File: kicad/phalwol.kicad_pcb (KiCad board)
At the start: 2 copper layers, 169.6 x 116.9 mm, 68 parts

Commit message: update pcb and schema
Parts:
- added REF**: D, yubuGadgetsFootpints:Diode_TH_SMD_REVERSIBLE, F.Cu at (134.7, 114.8)
- added REF**: D, yubuGadgetsFootpints:Diode_TH_SMD_REVERSIBLE, F.Cu at (106.2, 98.2)
- added REF**: D, yubuGadgetsFootpints:Diode_TH_SMD_REVERSIBLE, F.Cu at (134.8, 117.2)
- added REF**: D, yubuGadgetsFootpints:Diode_TH_SMD_REVERSIBLE, F.Cu at (158.5, 60.2)
- added REF**: D, yubuGadgetsFootpints:Diode_TH_SMD_REVERSIBLE, F.Cu at (144.2, 76.8)
- added REF**: D, yubuGadgetsFootpints:Diode_TH_SMD_REVERSIBLE, F.Cu at (101.5, 60.2)
- added REF**: D, yubuGadgetsFootpints:Diode_TH_SMD_REVERSIBLE, F.Cu at (182.2, 79.2)
- added REF**: D, yubuGadgetsFootpints:Diode_TH_SMD_REVERSIBLE, F.Cu at (144.2, 79.2)
- added REF**: D, yubuGadgetsFootpints:Diode_TH_SMD_REVERSIBLE, F.Cu at (125.2, 95.8)
- added REF**: D, yubuGadgetsFootpints:Diode_TH_SMD_REVERSIBLE, F.Cu at (139.5, 60.2)
- added REF**: D, yubuGadgetsFootpints:Diode_TH_SMD_REVERSIBLE, F.Cu at (106.2, 79.2)
- added REF**: D, yubuGadgetsFootpints:Diode_TH_SMD_REVERSIBLE, F.Cu at (101.5, 57.8)
- added REF**: D, yubuGadgetsFootpints:Diode_TH_SMD_REVERSIBLE, F.Cu at (163.2, 79.2)
- added REF**: D, yubuGadgetsFootpints:Diode_TH_SMD_REVERSIBLE, F.Cu at (172.8, 117.2)
- added REF**: D, yubuGadgetsFootpints:Diode_TH_SMD_REVERSIBLE, F.Cu at (144.2, 95.8)
- added REF**: D, yubuGadgetsFootpints:Diode_TH_SMD_REVERSIBLE, F.Cu at (106.2, 95.8)
- added REF**: D, yubuGadgetsFootpints:Diode_TH_SMD_REVERSIBLE, F.Cu at (120.5, 60.2)
- added REF**: D, yubuGadgetsFootpints:Diode_TH_SMD_REVERSIBLE, F.Cu at (177.5, 57.8)
- added REF**: D, yubuGadgetsFootpints:Diode_TH_SMD_REVERSIBLE, F.Cu at (125.2, 76.8)
- added REF**: D, yubuGadgetsFootpints:Diode_TH_SMD_REVERSIBLE, F.Cu at (158.5, 57.8)
- added REF**: D, yubuGadgetsFootpints:Diode_TH_SMD_REVERSIBLE, F.Cu at (163.2, 95.8)
- added REF**: D, yubuGadgetsFootpints:Diode_TH_SMD_REVERSIBLE, F.Cu at (153.8, 117.2)
- added REF**: D, yubuGadgetsFootpints:Diode_TH_SMD_REVERSIBLE, F.Cu at (191.7, 114.8)
- added REF**: D, yubuGadgetsFootpints:Diode_TH_SMD_REVERSIBLE, F.Cu at (177.5, 60.2)
- added REF**: D, yubuGadgetsFootpints:Diode_TH_SMD_REVERSIBLE, F.Cu at (172.7, 114.8)
- added REF**: D, yubuGadgetsFootpints:Diode_TH_SMD_REVERSIBLE, F.Cu at (139.5, 57.8)
- added REF**: D, yubuGadgetsFootpints:Diode_TH_SMD_REVERSIBLE, F.Cu at (153.7, 114.8)
- added REF**: D, yubuGadgetsFootpints:Diode_TH_SMD_REVERSIBLE, F.Cu at (182.2, 76.8)
- added REF**: D, yubuGadgetsFootpints:Diode_TH_SMD_REVERSIBLE, F.Cu at (106.2, 76.8)
- added REF**: D, yubuGadgetsFootpints:Diode_TH_SMD_REVERSIBLE, F.Cu at (115.7, 114.8)
- added REF**: D, yubuGadgetsFootpints:Diode_TH_SMD_REVERSIBLE, F.Cu at (120.5, 57.8)
- added REF**: D, yubuGadgetsFootpints:Diode_TH_SMD_REVERSIBLE, F.Cu at (144.2, 98.2)
- added REF**: D, yubuGadgetsFootpints:Diode_TH_SMD_REVERSIBLE, F.Cu at (163.2, 76.8)
- added REF**: D, yubuGadgetsFootpints:Diode_TH_SMD_REVERSIBLE, F.Cu at (163.2, 98.2)
- added REF**: D, yubuGadgetsFootpints:Diode_TH_SMD_REVERSIBLE, F.Cu at (115.8, 117.2)
- added REF**: D, yubuGadgetsFootpints:Diode_TH_SMD_REVERSIBLE, F.Cu at (182.2, 98.2)
- added REF**: D, yubuGadgetsFootpints:Diode_TH_SMD_REVERSIBLE, F.Cu at (125.2, 79.2)
- added REF**: D, yubuGadgetsFootpints:Diode_TH_SMD_REVERSIBLE, F.Cu at (182.2, 95.8)
- added REF**: D, yubuGadgetsFootpints:Diode_TH_SMD_REVERSIBLE, F.Cu at (125.2, 98.2)

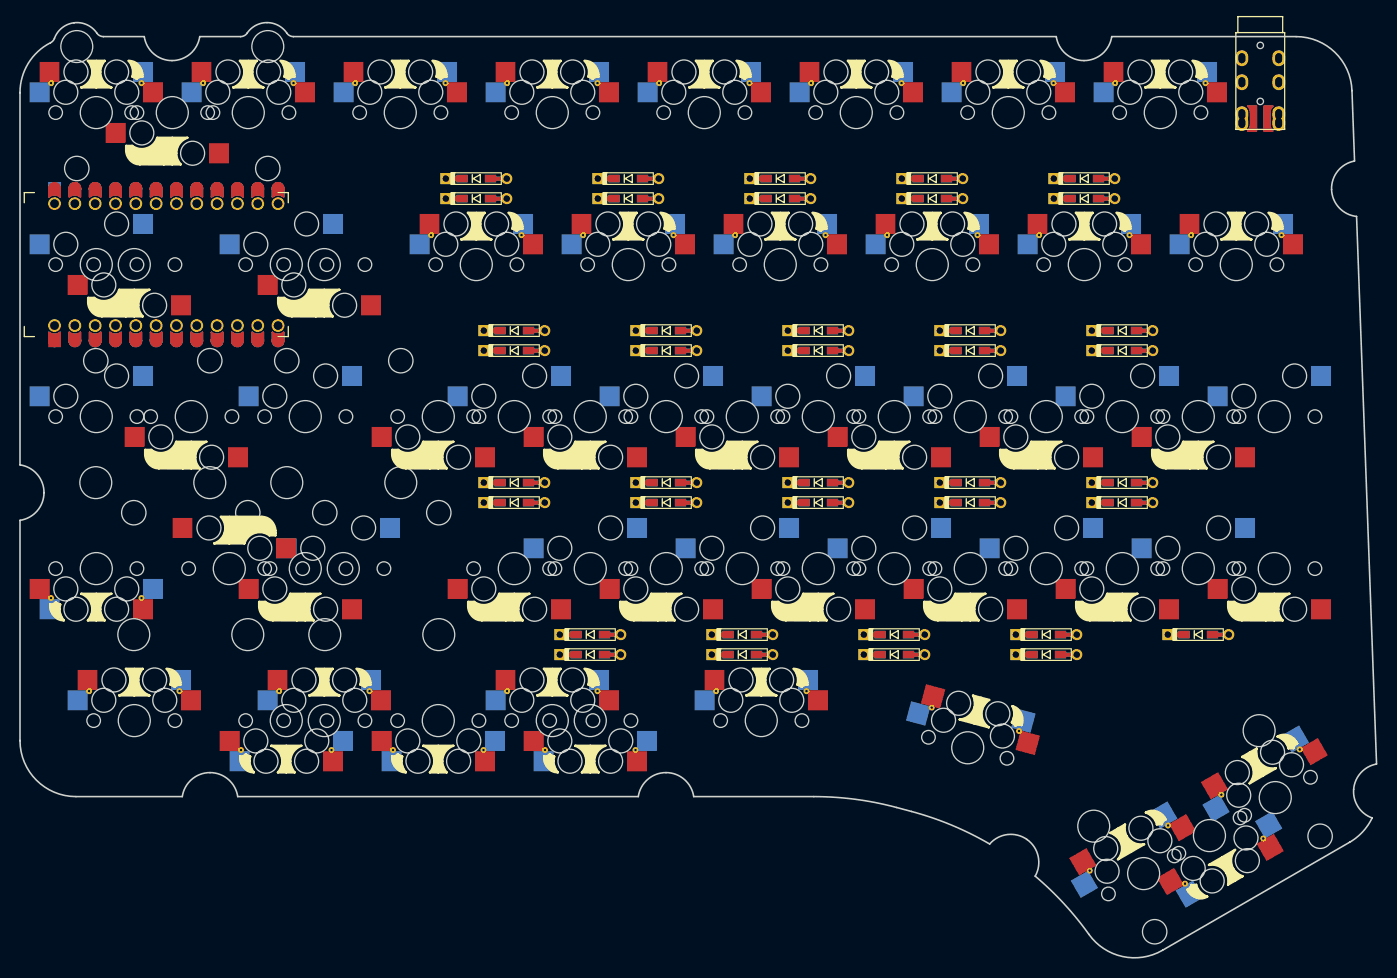
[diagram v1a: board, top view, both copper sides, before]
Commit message: connect schema and pcb
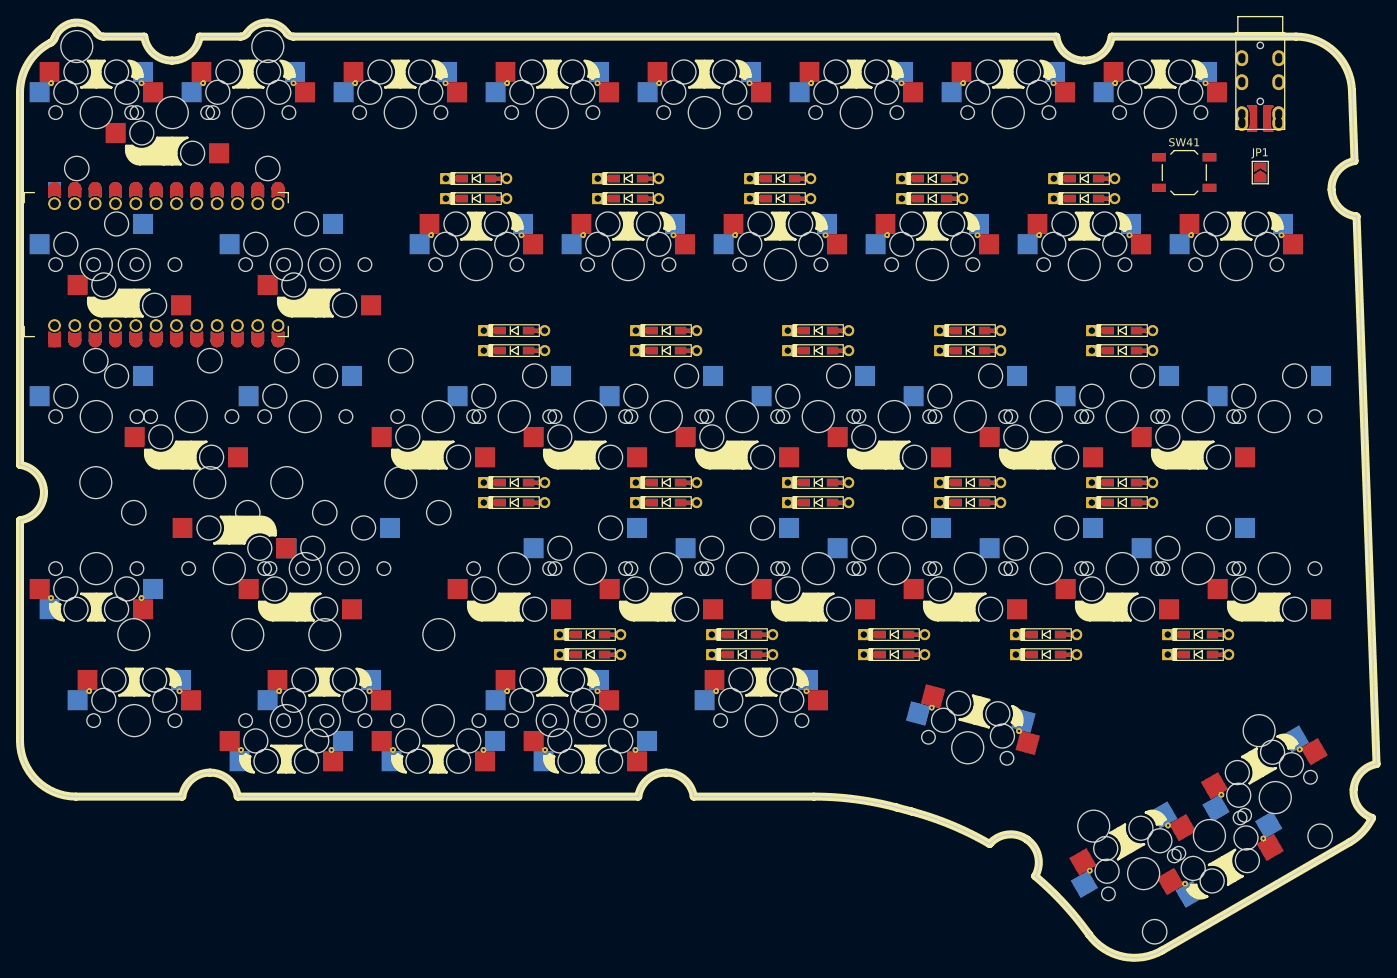
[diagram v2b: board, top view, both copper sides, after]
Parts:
- added D40: D, yubuGadgetsFootpints:Diode_TH_SMD_REVERSIBLE, F.Cu at (191.8, 117.2)
- added JP1: SolderJumper_2_Open, Jumper:SolderJumper-2_P1.3mm_Open_TrianglePad1.0x1.5mm, F.Cu at (199.5, 57.0)
- added JP2: SolderJumper_2_Open, Jumper:SolderJumper-2_P1.3mm_Open_TrianglePad1.0x1.5mm, B.Cu at (199.5, 57.0)
- added SW41: SW_Push, Button_Switch_SMD:SW_SPST_TL3342, F.Cu at (190.0, 57.0)
- added SW41: SW_Push, Button_Switch_SMD:SW_SPST_TL3342, B.Cu at (190.0, 57.0)
- J1: renamed from REF**; value TRRS-PJ-320A-ReversiblePad -> AudioJack4
- SW1 (x2), SW10 (x2), SW11, SW12, SW13, SW14, SW15, SW16, SW17 (x2), SW18, SW19 (x2), SW2, SW20 (x2), SW21 (x2), SW22 (x2), SW23 (x2), SW24 (x2), SW25, SW26 (x2), SW27 (x2), SW28 (x2), SW29 (x2), SW3, SW30 (x2), SW31 (x2), SW32, SW33, SW34 (x2), SW35 (x2), SW36, SW37, SW38, SW39 (x2), SW4, SW40, SW5, SW6, SW7, SW8, SW9 (x2): renamed from S*; value Val** -> SW_Push
- SW26: renamed from REF**; value Val** -> SW_Push
- renumbered REF** to D1, REF** to D10, REF** to D11, REF** to D12, REF** to D13, REF** to D14, REF** to D15, REF** to D16, REF** to D17, REF** to D18, REF** to D19, REF** to D2, REF** to D20, REF** to D21, REF** to D22, REF** to D23, REF** to D24, REF** to D25, REF** to D26, REF** to D27, REF** to D28, REF** to D29, REF** to D3, REF** to D30, REF** to D31, REF** to D32, REF** to D33, REF** to D34, REF** to D35, REF** to D36, REF** to D37, REF** to D38, REF** to D39, REF** to D4, REF** to D5, REF** to D6, REF** to D7, REF** to D8, REF** to D9, REF** to U1
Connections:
- D1 pad 1: (no net) -> ROW1
- D1 pad 2: (no net) -> Net-(D1-A)
- D10 pad 1: (no net) -> ROW2
- D10 pad 2: (no net) -> Net-(D10-A)
- D11 pad 1: (no net) -> ROW2
- D11 pad 2: (no net) -> Net-(D11-A)
- D12 pad 1: (no net) -> ROW2
- D12 pad 2: (no net) -> Net-(D12-A)
- D13 pad 1: (no net) -> ROW2
- D13 pad 2: (no net) -> Net-(D13-A)
- D14 pad 1: (no net) -> ROW2
- D14 pad 2: (no net) -> Net-(D14-A)
- D15 pad 1: (no net) -> ROW2
- D15 pad 2: (no net) -> Net-(D15-A)
- D16 pad 1: (no net) -> ROW2
- D16 pad 2: (no net) -> Net-(D16-A)
- D17 pad 1: (no net) -> ROW3
- D17 pad 2: (no net) -> Net-(D17-A)
- D18 pad 1: (no net) -> ROW3
- D18 pad 2: (no net) -> Net-(D18-A)
- D19 pad 1: (no net) -> ROW3
- D19 pad 2: (no net) -> Net-(D19-A)
- D2 pad 1: (no net) -> ROW1
- D2 pad 2: (no net) -> Net-(D2-A)
- D20 pad 1: (no net) -> ROW3
- D20 pad 2: (no net) -> Net-(D20-A)
- D21 pad 1: (no net) -> ROW3
- D21 pad 2: (no net) -> Net-(D21-A)
- D22 pad 1: (no net) -> ROW3
- D22 pad 2: (no net) -> Net-(D22-A)
- D23 pad 1: (no net) -> ROW3
- D23 pad 2: (no net) -> Net-(D23-A)
- D24 pad 1: (no net) -> ROW3
- D24 pad 2: (no net) -> Net-(D24-A)
- D25 pad 1: (no net) -> ROW4
- D25 pad 2: (no net) -> Net-(D25-A)
- D26 pad 1: (no net) -> ROW4
- D26 pad 2: (no net) -> Net-(D26-A)
- D27 pad 1: (no net) -> ROW4
- D27 pad 2: (no net) -> Net-(D27-A)
- D28 pad 1: (no net) -> ROW4
- D28 pad 2: (no net) -> Net-(D28-A)
- D29 pad 1: (no net) -> ROW4
- D29 pad 2: (no net) -> Net-(D29-A)
- D3 pad 1: (no net) -> ROW1
- D3 pad 2: (no net) -> Net-(D3-A)
- D30 pad 1: (no net) -> ROW4
- D30 pad 2: (no net) -> Net-(D30-A)
- D31 pad 1: (no net) -> ROW4
- D31 pad 2: (no net) -> Net-(D31-A)
- D32 pad 1: (no net) -> ROW4
- D32 pad 2: (no net) -> Net-(D32-A)
- D33 pad 1: (no net) -> ROW5
- D33 pad 2: (no net) -> Net-(D33-A)
- D34 pad 1: (no net) -> ROW5
- D34 pad 2: (no net) -> Net-(D34-A)
- D35 pad 1: (no net) -> ROW5
- D35 pad 2: (no net) -> Net-(D35-A)
- D36 pad 1: (no net) -> ROW5
- D36 pad 2: (no net) -> Net-(D36-A)
- D37 pad 1: (no net) -> ROW5
- D37 pad 2: (no net) -> Net-(D37-A)
- D38 pad 1: (no net) -> ROW5
- D38 pad 2: (no net) -> Net-(D38-A)
- D39 pad 1: (no net) -> ROW5
- D39 pad 2: (no net) -> Net-(D39-A)
- D4 pad 1: (no net) -> ROW1
- D4 pad 2: (no net) -> Net-(D4-A)
- D5 pad 1: (no net) -> ROW1
- D5 pad 2: (no net) -> Net-(D5-A)
- D6 pad 1: (no net) -> ROW1
- D6 pad 2: (no net) -> Net-(D6-A)
- D7 pad 1: (no net) -> ROW1
- D7 pad 2: (no net) -> Net-(D7-A)
- D8 pad 1: (no net) -> ROW1
- D8 pad 2: (no net) -> Net-(D8-A)
- D9 pad 1: (no net) -> ROW2
- D9 pad 2: (no net) -> Net-(D9-A)
- J1 pad R1: (no net) -> VCC
- J1 pad R2: (no net) -> GND
- J1 pad S: (no net) -> GND
- J1 pad T: (no net) -> SERIAL
- SW1 pad 1: (no net) -> COL1 (x2)
- SW1 pad 2: (no net) -> Net-(D1-A) (x2)
- SW10 pad 1: (no net) -> COL2 (x2)
- SW10 pad 2: (no net) -> Net-(D10-A) (x2)
- SW11 pad 1: (no net) -> COL3
- SW11 pad 2: (no net) -> Net-(D11-A)
- SW12 pad 1: (no net) -> COL4
- SW12 pad 2: (no net) -> Net-(D12-A)
- SW13 pad 1: (no net) -> COL5
- SW13 pad 2: (no net) -> Net-(D13-A)
- SW14 pad 1: (no net) -> COL6
- SW14 pad 2: (no net) -> Net-(D14-A)
- SW15 pad 1: (no net) -> COL7
- SW15 pad 2: (no net) -> Net-(D15-A)
- SW16 pad 1: (no net) -> COL8
- SW16 pad 2: (no net) -> Net-(D16-A)
- SW17 pad 1: (no net) -> COL1 (x2)
- SW17 pad 2: (no net) -> Net-(D17-A) (x2)
- SW18 pad 1: (no net) -> COL2
- SW18 pad 2: (no net) -> Net-(D18-A)
- SW19 pad 1: (no net) -> COL3 (x2)
- SW19 pad 2: (no net) -> Net-(D19-A) (x2)
- SW2 pad 1: (no net) -> COL2
- SW2 pad 2: (no net) -> Net-(D2-A)
- SW20 pad 1: (no net) -> COL4 (x2)
- SW20 pad 2: (no net) -> Net-(D20-A) (x2)
- SW21 pad 1: (no net) -> COL5 (x2)
- SW21 pad 2: (no net) -> Net-(D21-A) (x2)
- SW22 pad 1: (no net) -> COL6 (x2)
- SW22 pad 2: (no net) -> Net-(D22-A) (x2)
- SW23 pad 1: (no net) -> COL7 (x2)
- SW23 pad 2: (no net) -> Net-(D23-A) (x2)
- SW24 pad 1: (no net) -> COL8 (x2)
- SW24 pad 2: (no net) -> Net-(D24-A) (x2)
- SW25 pad 1: (no net) -> COL1
- SW25 pad 2: (no net) -> Net-(D25-A)
- SW26 pad 1: (no net) -> COL2 (x3)
- SW26 pad 2: (no net) -> Net-(D26-A) (x3)
- SW27 pad 1: (no net) -> COL3 (x2)
- SW27 pad 2: (no net) -> Net-(D27-A) (x2)
- SW28 pad 1: (no net) -> COL4 (x2)
- SW28 pad 2: (no net) -> Net-(D28-A) (x2)
- SW29 pad 1: (no net) -> COL5 (x2)
- SW29 pad 2: (no net) -> Net-(D29-A) (x2)
- SW3 pad 1: (no net) -> COL3
- SW3 pad 2: (no net) -> Net-(D3-A)
- SW30 pad 1: (no net) -> COL6 (x2)
- SW30 pad 2: (no net) -> Net-(D30-A) (x2)
- SW31 pad 1: (no net) -> COL7 (x2)
- SW31 pad 2: (no net) -> Net-(D31-A) (x2)
- SW32 pad 1: (no net) -> COL8
- SW32 pad 2: (no net) -> Net-(D32-A)
- SW33 pad 1: (no net) -> COL1
- SW33 pad 2: (no net) -> Net-(D33-A)
- SW34 pad 1: (no net) -> COL2 (x2)
- SW34 pad 2: (no net) -> Net-(D34-A) (x2)
- SW35 pad 1: (no net) -> COL3 (x2)
- SW35 pad 2: (no net) -> Net-(D35-A) (x2)
- SW36 pad 1: (no net) -> COL4
- SW36 pad 2: (no net) -> Net-(D36-A)
- SW37 pad 1: (no net) -> COL5
- SW37 pad 2: (no net) -> Net-(D37-A)
- SW38 pad 1: (no net) -> COL6
- SW38 pad 2: (no net) -> Net-(D38-A)
- SW39 pad 1: (no net) -> COL7 (x2)
- SW39 pad 2: (no net) -> Net-(D39-A) (x2)
- SW4 pad 1: (no net) -> COL4
- SW4 pad 2: (no net) -> Net-(D4-A)
- SW40 pad 1: (no net) -> COL8
- SW40 pad 2: (no net) -> Net-(D40-A)
- SW5 pad 1: (no net) -> COL5
- SW5 pad 2: (no net) -> Net-(D5-A)
- SW6 pad 1: (no net) -> COL6
- SW6 pad 2: (no net) -> Net-(D6-A)
- SW7 pad 1: (no net) -> COL7
- SW7 pad 2: (no net) -> Net-(D7-A)
- SW8 pad 1: (no net) -> COL8
- SW8 pad 2: (no net) -> Net-(D8-A)
- SW9 pad 1: (no net) -> COL1 (x2)
- SW9 pad 2: (no net) -> Net-(D9-A) (x2)
- U1 pad 1: (no net) -> unconnected-(U1-TX0/D3-Pad1)
- U1 pad 10: (no net) -> ROW3
- U1 pad 11: (no net) -> ROW2
- U1 pad 12: (no net) -> ROW1
- U1 pad 13: (no net) -> COL1
- U1 pad 14: (no net) -> COL2
- U1 pad 15: (no net) -> COL3
- U1 pad 16: (no net) -> COL4
- U1 pad 17: (no net) -> COL5
- U1 pad 18: (no net) -> COL6
- U1 pad 19: (no net) -> COL7
- U1 pad 2: (no net) -> SERIAL
- U1 pad 20: (no net) -> COL8
- U1 pad 21: (no net) -> VCC
- U1 pad 22: (no net) -> RST
- U1 pad 23: (no net) -> GND
- U1 pad 24: (no net) -> unconnected-(U1-RAW-Pad24)
- U1 pad 3: (no net) -> GND
- U1 pad 4: (no net) -> GND
- U1 pad 5: (no net) -> unconnected-(U1-2/D1/SDA-Pad5)
- U1 pad 6: (no net) -> unconnected-(U1-3/D0/SCL-Pad6)
- U1 pad 7: (no net) -> HAND
- U1 pad 8: (no net) -> ROW5
- U1 pad 9: (no net) -> ROW4

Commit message: update pcb
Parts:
- SW1, SW10 (x2), SW17 (x2), SW18, SW19 (x2), SW20 (x2), SW21 (x2), SW22 (x2), SW23 (x2), SW24 (x2), SW26 (x3), SW27 (x2), SW28 (x2), SW29 (x2), SW30 (x2), SW31 (x2), SW32, SW9 (x2): footprint yubuGadgetsFootpints:MX_HotswapOneside_Guided -> yubuGadgetsFootpints:MX_HotswapOneside_Via_Guided
- turned D1 to 180 degrees
- turned D10 to 180 degrees
- turned D11 to 180 degrees
- turned D12 to 180 degrees
- turned D13 to 180 degrees
- turned D14 to 180 degrees
- turned D15 to 180 degrees
- turned D16 to 180 degrees
- turned D17 to 180 degrees
- turned D18 to 180 degrees
- turned D19 to 180 degrees
- turned D2 to 180 degrees
- turned D20 to 180 degrees
- turned D21 to 180 degrees
- turned D22 to 180 degrees
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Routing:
- net COL1: track 0.00 -> 94.8 mm, vias 0 -> 1
- net ROW2: track 0.00 -> 58.1 mm, vias 0 -> 1
- net COL3: track 0.00 -> 57.1 mm, vias 0 -> 1
- net COL7: track 0.00 -> 55.7 mm, vias 0 -> 2
- net ROW3: track 0.00 -> 55.7 mm, vias 0 -> 1
- net ROW1: track 0.00 -> 54.7 mm, vias 0 -> 1
- net COL4: track 0.00 -> 54.0 mm, vias 0 -> 1
- net COL5: track 0.00 -> 51.8 mm, vias 0 -> 1
- net ROW4: track 0.00 -> 51.2 mm, vias 0 -> 1
- net COL6: track 0.00 -> 51.2 mm, vias 0 -> 1
- net ROW5: track 0.00 -> 50.6 mm, vias 0 -> 1
- net COL2: track 0.00 -> 39.3 mm, vias 0 -> 1
- net RST: track 0.00 -> 32.2 mm, vias 0 -> 1
- net VCC: track 0.00 -> 31.9 mm, vias 0 -> 1
- net unconnected-(U1-3/D0/SCL-Pad6): track 0.00 -> 23.9 mm, vias 0 -> 1
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
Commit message: Update phalwol.kicad_pcb
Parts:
- added SW26: SW_Push, yubuGadgetsFootpints:MX_HotswapOneside_Via_Guided, B.Cu at (75.4, 106.5)
- added SW27: SW_Push, yubuGadgetsFootpints:MX_HotswapOneside_Via_Guided, B.Cu at (96.8, 106.5)
- moved D8 100.3 mm to (196.5, 57.8)
- moved D7 97.4 mm to (196.5, 60.2)
- moved D6 82.0 mm to (177.5, 57.8)
- moved D5 79.6 mm to (177.5, 60.2)
- moved D16 77.9 mm to (201.2, 76.8)
- moved D15 75.4 mm to (201.2, 79.2)
- moved D25 73.3 mm to (115.8, 117.2)
- moved SW41 71.3 mm to (179.2, 127.5) (x2)
- moved D26 69.3 mm to (115.8, 114.8)
- moved D33 61.7 mm to (153.8, 114.8)
- moved D34 61.7 mm to (153.8, 117.2)
- moved D14 60.9 mm to (182.2, 76.8)
- moved D13 59.3 mm to (182.2, 79.2)
- moved D4 56.5 mm to (158.5, 57.8)
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- renumbered SW27 to SW28, SW28 to SW29, SW29 to SW30, SW30 to SW31, SW31 to SW32
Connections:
- SW28 pad 1: COL3 -> COL4
- SW28 pad 2: Net-(D27-A) -> Net-(D28-A)
- SW29 pad 1: COL4 -> COL5
- SW29 pad 2: Net-(D28-A) -> Net-(D29-A)
- SW30 pad 1: COL5 -> COL6
- SW30 pad 2: Net-(D29-A) -> Net-(D30-A)
- SW31 pad 1: COL6 -> COL7
- SW31 pad 2: Net-(D30-A) -> Net-(D31-A)
- SW32 pad 1: COL7 -> COL8
- SW32 pad 2: Net-(D31-A) -> Net-(D32-A)
- SW34 pad 1: COL2 -> Net-(D34-A)
- SW34 pad 2: Net-(D34-A) -> COL2
- SW35 pad 1: COL3 -> Net-(D35-A)
- SW35 pad 2: Net-(D35-A) -> COL3
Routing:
- net Net-(D9-A): track 9.21 -> 114.0 mm
- net Net-(D33-A): track 0.00 -> 89.2 mm, vias 1 -> 0
- net Net-(D1-A): track 13.1 -> 96.7 mm, vias 1 -> 0
- net Net-(D10-A): track 9.21 -> 83.3 mm
- net Net-(D35-A): track 0.00 -> 73.5 mm, vias 1 -> 0
- net Net-(D34-A): track 0.00 -> 73.2 mm, vias 1 -> 0
- net Net-(D36-A): track 0.00 -> 69.1 mm, vias 1 -> 0
- net Net-(D37-A): track 0.00 -> 64.7 mm, vias 1 -> 0
- net Net-(D3-A): track 0.00 -> 61.1 mm, vias 1 -> 0
- net Net-(D2-A): track 0.00 -> 60.1 mm, vias 1 -> 0
- net Net-(D11-A): track 0.00 -> 56.4 mm, vias 1 -> 0
- net Net-(D25-A): track 0.00 -> 54.4 mm, vias 1 -> 0
- net Net-(D17-A): track 16.3 -> 64.4 mm, vias 1 -> 0
- net Net-(D29-A): track 15.4 -> 60.8 mm, vias 1 -> 0
- net Net-(D5-A): track 0.00 -> 42.1 mm, vias 1 -> 0
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
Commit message: Update phalwol.kicad_pcb
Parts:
- moved JP1 0.39 mm to (205.8, 47.5)
- moved JP2 0.39 mm to (205.8, 47.5)
- moved D31 0.12 mm to (201.2, 95.8)
- moved D32 0.12 mm to (201.3, 98.2)
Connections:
- U1 pad 11: ROW2 -> ROW4
- U1 pad 12: ROW1 -> ROW5
- U1 pad 13: COL1 -> COL8
- U1 pad 14: COL2 -> COL7
- U1 pad 15: COL3 -> COL6
- U1 pad 16: COL4 -> COL5
- U1 pad 17: COL5 -> COL4
- U1 pad 18: COL6 -> COL3
- U1 pad 19: COL7 -> COL2
- U1 pad 20: COL8 -> COL1
- U1 pad 8: ROW5 -> ROW1
- U1 pad 9: ROW4 -> ROW2
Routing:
- net COL7: track 56.1 -> 295.2 mm, vias 1 -> 4
- net COL8: track 56.8 -> 270.4 mm, vias 1 -> 4
- net COL6: track 52.2 -> 222.8 mm, vias 1 -> 4
- net SERIAL: track 22.3 -> 190.9 mm, vias 1 -> 4
- net VCC: track 29.6 -> 192.9 mm, vias 1 -> 4
- net HAND: track 22.1 -> 183.9 mm, vias 1 -> 4
- net COL5: track 52.1 -> 199.5 mm, vias 1 -> 3
- net COL2: track 47.5 -> 187.9 mm
- net COL4: track 53.1 -> 177.8 mm, vias 1 -> 3
- net Net-(D16-A): track 13.3 -> 126.2 mm
- net Net-(D8-A): track 11.4 -> 123.5 mm
- net COL3: track 75.1 -> 173.1 mm, vias 1 -> 3
- net Net-(D15-A): track 18.6 -> 109.2 mm
- net Net-(D7-A): track 23.1 -> 106.5 mm
- net Net-(D14-A): track 17.3 -> 70.2 mm
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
